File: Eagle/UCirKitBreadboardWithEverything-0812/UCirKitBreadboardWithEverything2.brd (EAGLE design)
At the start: 72.8 x 99.4 mm, 900 parts

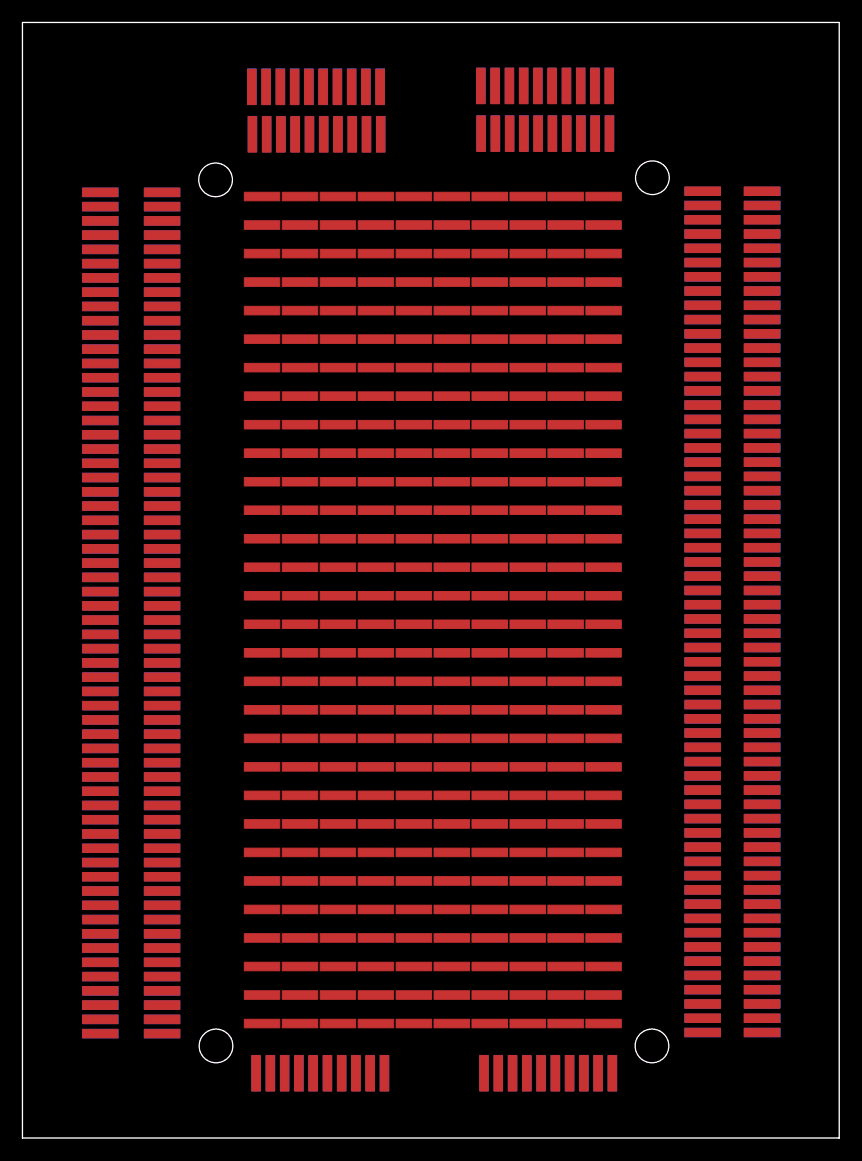
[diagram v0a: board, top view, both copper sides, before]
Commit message: UCirKitEverything2Top is OK for Routing, UCirKitEverything2 is not OK. Look for UCirKitEverything2 for Bottom part
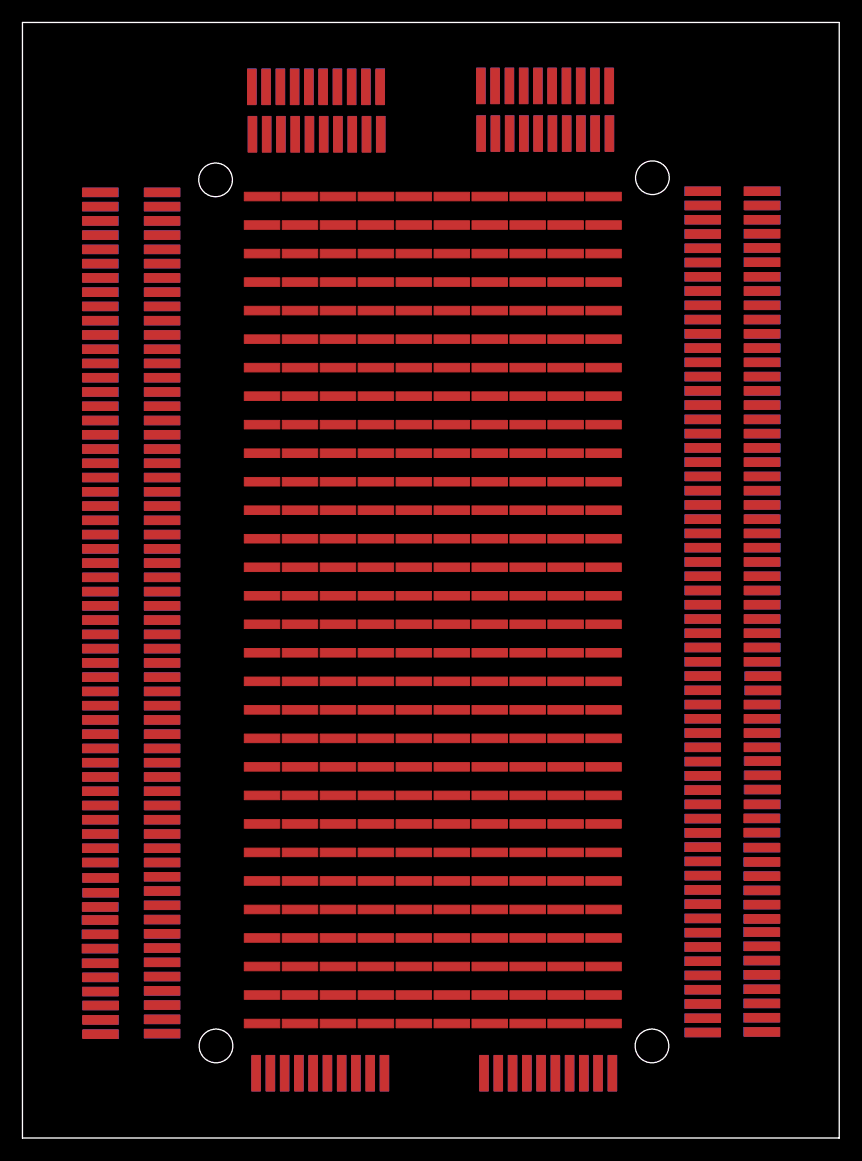
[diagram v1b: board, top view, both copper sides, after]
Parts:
- moved JP1080 16.5 mm to (65.8, 25.9), turned to 180 degrees
- moved JP780 16.5 mm to (65.9, 25.9), turned to 180 degrees
- moved JP1079 13.9 mm to (65.8, 24.6), turned to 180 degrees
- moved JP779 13.9 mm to (65.9, 24.6), turned to 180 degrees
- moved JP1069 13.9 mm to (65.8, 9.45), turned to 180 degrees
- moved JP769 13.9 mm to (65.9, 9.45), turned to 180 degrees
- moved JP1065 13.9 mm to (65.8, 14.5), turned to 180 degrees
- moved JP765 13.9 mm to (65.9, 14.5), turned to 180 degrees
- moved JP720 12.5 mm to (6.97, 21.8), turned to 180 degrees
- moved JP1140 12.5 mm to (6.94, 21.8), turned to 180 degrees
- moved JP1078 11.4 mm to (65.8, 23.3), turned to 180 degrees
- moved JP778 11.4 mm to (65.9, 23.3), turned to 180 degrees
- moved JP1070 11.4 mm to (65.8, 10.7), turned to 180 degrees
- moved JP770 11.4 mm to (65.9, 10.7), turned to 180 degrees
- moved JP1066 11.4 mm to (65.8, 15.8), turned to 180 degrees
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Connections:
- new net 0_1439897169: JP301.P$3, JP841.P$3
- new net 0_1439897178: JP311.P$3, JP843.P$3
- new net 0_1439897188: JP321.P$3, JP845.P$3
- new net 0_1439897194: JP310.P$3, JP781.P$3
- new net 0_1439897209: JP320.P$3, JP783.P$3
- new net 0_1439897217: JP330.P$3, JP785.P$3
- new net 0_1439897230: JP340.P$3, JP787.P$3
- new net 0_1439897238: JP350.P$3, JP789.P$3
- new net 0_1439897247: JP360.P$3, JP791.P$3
- new net 0_1439897254: JP370.P$3, JP793.P$3
- new net 0_1439897261: JP380.P$3, JP795.P$3
- new net 0_1439897267: JP390.P$3, JP797.P$3
- new net 0_1439897281: JP600.P$3, JP839.P$3
- new net 0_1439897288: JP590.P$3, JP837.P$3
- new net 0_1439897294: JP580.P$3, JP835.P$3
- new net 0_1439897300: JP591.P$3, JP899.P$3
- new net 0_1439897307: JP581.P$3, JP897.P$3
- new net 0_1439897312: JP571.P$3, JP895.P$3
- new net 0_1439897321: JP561.P$3, JP893.P$3
- new net 0_1439897329: JP551.P$3, JP891.P$3
- new net 0_1439897335: JP541.P$3, JP889.P$3
- new net 0_1439897341: JP531.P$3, JP887.P$3
- new net 0_1439897349: JP521.P$3, JP885.P$3
- new net 0_1439897354: JP570.P$3, JP833.P$3
- new net 0_1439897362: JP560.P$3, JP831.P$3
- new net 0_1439897369: JP550.P$3, JP829.P$3
- new net 0_1439897383: JP540.P$3, JP827.P$3
- new net 0_1439897389: JP530.P$3, JP825.P$3
- new net 0_1439897395: JP511.P$3, JP883.P$3
- new net 0_1439897401: JP501.P$3, JP881.P$3
- new net 0_1439897407: JP491.P$3, JP879.P$3
- new net 0_1439897412: JP481.P$3, JP877.P$3
- new net 0_1439897418: JP471.P$3, JP875.P$3
- new net 0_1439897423: JP461.P$3, JP873.P$3
- new net 0_1439897429: JP451.P$3, JP871.P$3
- new net 0_1439897436: JP520.P$3, JP823.P$3
- new net 0_1439897442: JP510.P$3, JP821.P$3
- new net 0_1439897448: JP500.P$3, JP819.P$3
- new net 0_1439897454: JP490.P$3, JP817.P$3
- new net 0_1439897461: JP480.P$3, JP815.P$3
- new net 0_1439897467: JP470.P$3, JP813.P$3
- new net 0_1439897473: JP460.P$3, JP811.P$3
- new net 0_1439897480: JP450.P$3, JP809.P$3
- new net 0_1439897485: JP441.P$3, JP869.P$3
- new net 0_1439897491: JP431.P$3, JP867.P$3
- new net 0_1439897496: JP421.P$3, JP865.P$3
- new net 0_1439897505: JP411.P$3, JP863.P$3
- new net 0_1439897514: JP401.P$3, JP861.P$3
- new net 0_1439897520: JP440.P$3, JP807.P$3
- new net 0_1439897527: JP430.P$3, JP805.P$3
- new net 0_1439897534: JP420.P$3, JP803.P$3
- new net 0_1439897539: JP410.P$3, JP801.P$3
- new net 0_1439897546: JP400.P$3, JP799.P$3
- new net 0_1439897614: JP391.P$3, JP859.P$3
- new net 0_1439897622: JP381.P$3, JP857.P$3
- new net 0_1439897631: JP371.P$3, JP855.P$3
- new net 0_1439897637: JP361.P$3, JP853.P$3
- new net 0_1439897643: JP351.P$3, JP851.P$3
- new net 0_1439897654: JP331.P$3, JP847.P$3
- new net 0_1439897660: JP341.P$3, JP849.P$3
- new net 0_1439897711: JP593.P$3, JP651.P$3
- new net 0_1439897726: JP597.P$3, JP641.P$3
- new net 0_1439897746: JP303.P$3, JP621.P$3
- new net 0_1439897770: JP307.P$3, JP601.P$3
- new net 0_1439897792: JP363.P$3, JP661.P$3
- new net 0_1439897815: JP378.P$3, JP721.P$3
- new net 0_1439897831: JP473.P$3, JP695.P$3
- new net 0_1439897845: JP488.P$3, JP757.P$3
- new net 0_1439897966: JP423.P$3, JP677.P$3
- new net 0_1439897993: JP428.P$3, JP737.P$3
- new net 10_1439897746: JP333.P$3, JP631.P$3
- new net 10_1439897770: JP326.P$3, JP611.P$3
- new net 10_1439897792: JP375.P$3, JP671.P$3
- new net 10_1439897815: JP376.P$3, JP731.P$3
- new net 10_1439897831: JP524.P$3, JP705.P$3
- new net 10_1439897845: JP537.P$3, JP767.P$3
- new net 10_1439897966: JP474.P$3, JP687.P$3
- new net 10_1439897993: JP467.P$3, JP747.P$3
- new net 11_1439897746: JP343.P$3, JP632.P$3
- new net 11_1439897770: JP336.P$3, JP612.P$3
- new net 11_1439897792: JP414.P$3, JP672.P$3
- new net 11_1439897815: JP417.P$3, JP732.P$3
- new net 11_1439897831: JP534.P$3, JP706.P$3
- new net 11_1439897845: JP527.P$3, JP768.P$3
- new net 11_1439897966: JP435.P$3, JP688.P$3
- new net 11_1439897993: JP477.P$3, JP748.P$3
- new net 12_1439897746: JP335.P$3, JP633.P$3
- new net 12_1439897770: JP348.P$3, JP613.P$3
- new net 12_1439897792: JP385.P$3, JP673.P$3
- new net 12_1439897815: JP386.P$3, JP733.P$3
- new net 12_1439897831: JP544.P$3, JP707.P$3
- new net 12_1439897845: JP576.P$3, JP769.P$3
- new net 12_1439897966: JP445.P$3, JP689.P$3
- new net 12_1439897993: JP446.P$3, JP749.P$3
- new net 13_1439897746: JP344.P$3, JP634.P$3
- new net 13_1439897770: JP347.P$3, JP614.P$3
- new net 13_1439897792: JP395.P$3, JP674.P$3
- new net 13_1439897815: JP396.P$3, JP734.P$3
- new net 13_1439897831: JP554.P$3, JP708.P$3
- new net 13_1439897845: JP566.P$3, JP770.P$3
- new net 13_1439897966: JP455.P$3, JP690.P$3
- new net 13_1439897993: JP456.P$3, JP750.P$3
- new net 14_1439897746: JP345.P$3, JP635.P$3
- new net 14_1439897770: JP346.P$3, JP615.P$3
- new net 14_1439897792: JP405.P$3, JP675.P$3
- new net 14_1439897815: JP406.P$3, JP735.P$3
- new net 14_1439897831: JP514.P$3, JP709.P$3
- new net 14_1439897845: JP556.P$3, JP771.P$3
- new net 14_1439897966: JP465.P$3, JP691.P$3
- new net 14_1439897993: JP466.P$3, JP751.P$3
- new net 15_1439897746: JP353.P$3, JP636.P$3
- new net 15_1439897770: JP358.P$3, JP616.P$3
- new net 15_1439897792: JP415.P$3, JP676.P$3
- new net 15_1439897815: JP416.P$3, JP736.P$3
- new net 15_1439897831: JP504.P$3, JP710.P$3
- new net 15_1439897845: JP546.P$3, JP772.P$3
- new net 15_1439897966: JP475.P$3, JP692.P$3
- new net 15_1439897993: JP476.P$3, JP752.P$3
- new net 16_1439897746: JP354.P$3, JP637.P$3
- new net 16_1439897770: JP357.P$3, JP617.P$3
- new net 16_1439897831: JP545.P$3, JP711.P$3
- new net 16_1439897845: JP517.P$3, JP773.P$3
- new net 16_1439897966: JP485.P$3, JP693.P$3
- new net 16_1439897993: JP486.P$3, JP753.P$3
- new net 17_1439897746: JP355.P$3, JP638.P$3
- new net 17_1439897770: JP356.P$3, JP618.P$3
- new net 17_1439897831: JP555.P$3, JP712.P$3
- new net 17_1439897845: JP507.P$3, JP774.P$3
- new net 17_1439897966: JP425.P$3, JP694.P$3
- new net 17_1439897993: JP496.P$3, JP754.P$3
- new net 18_1439897746: JP364.P$3, JP639.P$3
- new net 18_1439897770: JP368.P$3, JP619.P$3
- new net 18_1439897831: JP565.P$3, JP713.P$3
- new net 18_1439897845: JP536.P$3, JP775.P$3
- new net 18_1439897993: JP436.P$3, JP755.P$3
- new net 19_1439897746: JP365.P$3, JP640.P$3
- new net 19_1439897770: JP367.P$3, JP620.P$3
- new net 19_1439897831: JP535.P$3, JP714.P$3
- new net 19_1439897845: JP497.P$3, JP776.P$3
- new net 19_1439897993: JP426.P$3, JP756.P$3
- new net 1_1439897169: JP302.P$3, JP842.P$3
- new net 1_1439897178: JP312.P$3, JP844.P$3
- new net 1_1439897188: JP322.P$3, JP846.P$3
- new net 1_1439897194: JP309.P$3, JP782.P$3
- new net 1_1439897209: JP319.P$3, JP784.P$3
- new net 1_1439897217: JP329.P$3, JP786.P$3
- new net 1_1439897230: JP339.P$3, JP788.P$3
- new net 1_1439897238: JP349.P$3, JP790.P$3
- new net 1_1439897247: JP359.P$3, JP792.P$3
- new net 1_1439897254: JP369.P$3, JP794.P$3
- new net 1_1439897261: JP379.P$3, JP796.P$3
- new net 1_1439897267: JP389.P$3, JP798.P$3
- new net 1_1439897281: JP599.P$3, JP840.P$3
- new net 1_1439897288: JP589.P$3, JP838.P$3
- new net 1_1439897294: JP579.P$3, JP836.P$3
- new net 1_1439897300: JP592.P$3, JP900.P$3
- new net 1_1439897307: JP582.P$3, JP898.P$3
- new net 1_1439897312: JP572.P$3, JP896.P$3
- new net 1_1439897321: JP562.P$3, JP894.P$3
- new net 1_1439897329: JP552.P$3, JP892.P$3
- new net 1_1439897335: JP542.P$3, JP890.P$3
- new net 1_1439897341: JP532.P$3, JP888.P$3
- new net 1_1439897349: JP522.P$3, JP886.P$3
- new net 1_1439897354: JP569.P$3, JP834.P$3
- new net 1_1439897362: JP559.P$3, JP832.P$3
- new net 1_1439897369: JP549.P$3, JP830.P$3
- new net 1_1439897383: JP539.P$3, JP828.P$3
- new net 1_1439897389: JP529.P$3, JP826.P$3
- new net 1_1439897395: JP512.P$3, JP884.P$3
- new net 1_1439897401: JP502.P$3, JP882.P$3
- new net 1_1439897407: JP492.P$3, JP880.P$3
- new net 1_1439897412: JP482.P$3, JP878.P$3
- new net 1_1439897418: JP472.P$3, JP876.P$3
- new net 1_1439897423: JP462.P$3, JP874.P$3
- new net 1_1439897429: JP452.P$3, JP872.P$3
- new net 1_1439897436: JP519.P$3, JP824.P$3
- new net 1_1439897442: JP509.P$3, JP822.P$3
- new net 1_1439897448: JP499.P$3, JP820.P$3
- new net 1_1439897454: JP489.P$3, JP818.P$3
- new net 1_1439897461: JP479.P$3, JP816.P$3
- new net 1_1439897467: JP469.P$3, JP814.P$3
- new net 1_1439897473: JP459.P$3, JP812.P$3
- new net 1_1439897480: JP449.P$3, JP810.P$3
- new net 1_1439897485: JP442.P$3, JP870.P$3
- new net 1_1439897491: JP432.P$3, JP868.P$3
- new net 1_1439897496: JP422.P$3, JP866.P$3
- new net 1_1439897505: JP412.P$3, JP864.P$3
- new net 1_1439897514: JP402.P$3, JP862.P$3
- new net 1_1439897520: JP439.P$3, JP808.P$3
- new net 1_1439897527: JP429.P$3, JP806.P$3
- new net 1_1439897534: JP419.P$3, JP804.P$3
- new net 1_1439897539: JP409.P$3, JP802.P$3
- new net 1_1439897546: JP399.P$3, JP800.P$3
- new net 1_1439897614: JP392.P$3, JP860.P$3
- new net 1_1439897622: JP382.P$3, JP858.P$3
- new net 1_1439897631: JP372.P$3, JP856.P$3
- new net 1_1439897637: JP362.P$3, JP854.P$3
- new net 1_1439897643: JP352.P$3, JP852.P$3
- new net 1_1439897654: JP332.P$3, JP848.P$3
- new net 1_1439897660: JP342.P$3, JP850.P$3
- new net 1_1439897711: JP583.P$3, JP652.P$3
- new net 1_1439897726: JP598.P$3, JP642.P$3
- new net 1_1439897746: JP304.P$3, JP622.P$3
- new net 1_1439897770: JP308.P$3, JP602.P$3
- new net 1_1439897792: JP373.P$3, JP662.P$3
- new net 1_1439897815: JP388.P$3, JP722.P$3
- new net 1_1439897831: JP483.P$3, JP696.P$3
- new net 1_1439897845: JP498.P$3, JP758.P$3
- new net 1_1439897966: JP433.P$3, JP678.P$3
- new net 1_1439897993: JP438.P$3, JP738.P$3
- new net 20_1439897831: JP525.P$3, JP715.P$3
- new net 20_1439897845: JP526.P$3, JP777.P$3
- new net 21_1439897831: JP494.P$3, JP716.P$3
- new net 21_1439897845: JP487.P$3, JP778.P$3
- new net 22_1439897831: JP515.P$3, JP717.P$3
- new net 22_1439897845: JP516.P$3, JP779.P$3
- new net 23_1439897831: JP505.P$3, JP718.P$3
- new net 23_1439897845: JP506.P$3, JP780.P$3
- new net 24_1439897831: JP484.P$3, JP719.P$3
- new net 25_1439897831: JP495.P$3, JP720.P$3
- new net 2_1439897711: JP594.P$3, JP653.P$3
- new net 2_1439897726: JP596.P$3, JP643.P$3
- new net 2_1439897746: JP313.P$3, JP623.P$3
- new net 2_1439897770: JP306.P$3, JP603.P$3
- new net 2_1439897792: JP383.P$3, JP663.P$3
- new net 2_1439897815: JP377.P$3, JP723.P$3
- new net 2_1439897831: JP493.P$3, JP697.P$3
- new net 2_1439897845: JP508.P$3, JP759.P$3
- new net 2_1439897966: JP443.P$3, JP679.P$3
- new net 2_1439897993: JP448.P$3, JP739.P$3
- new net 3_1439897711: JP584.P$3, JP654.P$3
- new net 3_1439897726: JP588.P$3, JP644.P$3
- new net 3_1439897746: JP314.P$3, JP624.P$3
- new net 3_1439897770: JP318.P$3, JP604.P$3
- new net 3_1439897792: JP374.P$3, JP664.P$3
- new net 3_1439897815: JP398.P$3, JP724.P$3
- new net 3_1439897831: JP503.P$3, JP698.P$3
- new net 3_1439897845: JP518.P$3, JP760.P$3
- new net 3_1439897966: JP424.P$3, JP680.P$3
- new net 3_1439897993: JP427.P$3, JP740.P$3
- new net 4_1439897711: JP573.P$3, JP655.P$3
- new net 4_1439897726: JP587.P$3, JP645.P$3
- new net 4_1439897746: JP305.P$3, JP625.P$3
- new net 4_1439897770: JP317.P$3, JP605.P$3
- new net 4_1439897792: JP393.P$3, JP665.P$3
- new net 4_1439897815: JP387.P$3, JP725.P$3
- new net 4_1439897831: JP513.P$3, JP699.P$3
- new net 4_1439897845: JP528.P$3, JP761.P$3
- new net 4_1439897966: JP453.P$3, JP681.P$3
- new net 4_1439897993: JP458.P$3, JP741.P$3
- new net 5_1439897711: JP595.P$3, JP656.P$3
- new net 5_1439897726: JP578.P$3, JP646.P$3
- new net 5_1439897746: JP315.P$3, JP626.P$3
- new net 5_1439897770: JP328.P$3, JP606.P$3
- new net 5_1439897792: JP384.P$3, JP666.P$3
- new net 5_1439897815: JP366.P$3, JP726.P$3
- new net 5_1439897831: JP523.P$3, JP700.P$3
- new net 5_1439897845: JP538.P$3, JP762.P$3
- new net 5_1439897966: JP434.P$3, JP682.P$3
- new net 5_1439897993: JP437.P$3, JP742.P$3
- new net 6_1439897711: JP585.P$3, JP657.P$3
- new net 6_1439897726: JP577.P$3, JP647.P$3
- new net 6_1439897746: JP323.P$3, JP627.P$3
- new net 6_1439897770: JP327.P$3, JP607.P$3
- new net 6_1439897792: JP403.P$3, JP667.P$3
- new net 6_1439897815: JP408.P$3, JP727.P$3
- new net 6_1439897831: JP533.P$3, JP701.P$3
- new net 6_1439897845: JP548.P$3, JP763.P$3
- new net 6_1439897966: JP463.P$3, JP683.P$3
- new net 6_1439897993: JP468.P$3, JP743.P$3
- new net 7_1439897711: JP574.P$3, JP658.P$3
- new net 7_1439897726: JP568.P$3, JP648.P$3
- new net 7_1439897746: JP324.P$3, JP628.P$3
- new net 7_1439897770: JP338.P$3, JP608.P$3
- new net 7_1439897792: JP394.P$3, JP668.P$3
- new net 7_1439897815: JP397.P$3, JP728.P$3
- new net 7_1439897831: JP543.P$3, JP702.P$3
- new net 7_1439897845: JP558.P$3, JP764.P$3
- new net 7_1439897966: JP444.P$3, JP684.P$3
- new net 7_1439897993: JP447.P$3, JP744.P$3
- new net 8_1439897711: JP575.P$3, JP659.P$3
- new net 8_1439897726: JP586.P$3, JP649.P$3
- new net 8_1439897746: JP325.P$3, JP629.P$3
- new net 8_1439897770: JP316.P$3, JP609.P$3
- new net 8_1439897792: JP413.P$3, JP669.P$3
- new net 8_1439897815: JP418.P$3, JP729.P$3
- new net 8_1439897831: JP553.P$3, JP703.P$3
- new net 8_1439897845: JP557.P$3, JP765.P$3
- new net 8_1439897966: JP454.P$3, JP685.P$3
- new net 8_1439897993: JP478.P$3, JP745.P$3
- new net 9_1439897711: JP564.P$3, JP660.P$3
- new net 9_1439897726: JP567.P$3, JP650.P$3
- new net 9_1439897746: JP334.P$3, JP630.P$3
- new net 9_1439897770: JP337.P$3, JP610.P$3
- new net 9_1439897792: JP404.P$3, JP670.P$3
- new net 9_1439897815: JP407.P$3, JP730.P$3
- new net 9_1439897831: JP563.P$3, JP704.P$3
- new net 9_1439897845: JP547.P$3, JP766.P$3
- new net 9_1439897966: JP464.P$3, JP686.P$3
- new net 9_1439897993: JP457.P$3, JP746.P$3
- new net CLEAN600: JP901.P$3
- new net CLEAN601: JP902.P$3
- new net CLEAN602: JP903.P$3
- new net CLEAN603: JP904.P$3
- new net CLEAN604: JP905.P$3
- new net CLEAN605: JP906.P$3
- new net CLEAN606: JP907.P$3
- new net CLEAN607: JP908.P$3
- new net CLEAN608: JP909.P$3
- new net CLEAN609: JP910.P$3
- new net CLEAN610: JP911.P$3
- new net CLEAN611: JP912.P$3
- new net CLEAN612: JP913.P$3
- new net CLEAN613: JP914.P$3
- new net CLEAN614: JP915.P$3
- new net CLEAN615: JP916.P$3
- new net CLEAN616: JP917.P$3
- new net CLEAN617: JP918.P$3
- new net CLEAN618: JP919.P$3
- new net CLEAN619: JP920.P$3
- new net CLEAN620: JP921.P$3
- new net CLEAN621: JP922.P$3
- new net CLEAN622: JP923.P$3
- new net CLEAN623: JP924.P$3
- new net CLEAN624: JP925.P$3
- new net CLEAN625: JP926.P$3
- new net CLEAN626: JP927.P$3
- new net CLEAN627: JP928.P$3
- new net CLEAN628: JP929.P$3
- new net CLEAN629: JP930.P$3
- new net CLEAN630: JP931.P$3
- new net CLEAN631: JP932.P$3
- new net CLEAN632: JP933.P$3
- new net CLEAN633: JP934.P$3
- new net CLEAN634: JP935.P$3
- new net CLEAN635: JP936.P$3
- new net CLEAN636: JP937.P$3
- new net CLEAN637: JP938.P$3
- new net CLEAN638: JP939.P$3
- new net CLEAN639: JP940.P$3
- new net CLEAN640: JP941.P$3
- new net CLEAN641: JP942.P$3
- new net CLEAN642: JP943.P$3
- new net CLEAN643: JP944.P$3
- new net CLEAN644: JP945.P$3
- new net CLEAN645: JP946.P$3
- new net CLEAN646: JP947.P$3
- new net CLEAN647: JP948.P$3
- new net CLEAN648: JP949.P$3
- new net CLEAN649: JP950.P$3
- new net CLEAN650: JP951.P$3
- new net CLEAN651: JP952.P$3
- new net CLEAN652: JP953.P$3
- new net CLEAN653: JP954.P$3
- new net CLEAN654: JP955.P$3
- new net CLEAN655: JP956.P$3
- new net CLEAN656: JP957.P$3
- new net CLEAN657: JP958.P$3
- new net CLEAN658: JP959.P$3
- new net CLEAN659: JP960.P$3
- new net CLEAN660: JP961.P$3
- new net CLEAN661: JP962.P$3
- new net CLEAN662: JP963.P$3
- new net CLEAN663: JP964.P$3
- new net CLEAN664: JP965.P$3
- new net CLEAN665: JP966.P$3
- new net CLEAN666: JP967.P$3
- new net CLEAN667: JP968.P$3
- new net CLEAN668: JP969.P$3
- new net CLEAN669: JP970.P$3
- new net CLEAN670: JP971.P$3
- new net CLEAN671: JP972.P$3
- new net CLEAN672: JP973.P$3
- new net CLEAN673: JP974.P$3
- new net CLEAN674: JP975.P$3
- new net CLEAN675: JP976.P$3
- new net CLEAN676: JP977.P$3
- new net CLEAN677: JP978.P$3
- new net CLEAN678: JP979.P$3
- new net CLEAN679: JP980.P$3
- new net CLEAN680: JP981.P$3
- new net CLEAN681: JP982.P$3
- new net CLEAN682: JP983.P$3
- new net CLEAN683: JP984.P$3
- new net CLEAN684: JP985.P$3
- new net CLEAN685: JP986.P$3
- new net CLEAN686: JP987.P$3
- new net CLEAN687: JP988.P$3
- new net CLEAN688: JP989.P$3
- new net CLEAN689: JP990.P$3
- new net CLEAN690: JP991.P$3
- new net CLEAN691: JP992.P$3
- new net CLEAN692: JP993.P$3
- new net CLEAN693: JP994.P$3
- new net CLEAN694: JP995.P$3
- new net CLEAN695: JP996.P$3
- new net CLEAN696: JP997.P$3
- new net CLEAN697: JP998.P$3
- new net CLEAN698: JP999.P$3
- new net CLEAN699: JP1000.P$3
- new net CLEAN700: JP1001.P$3
- new net CLEAN701: JP1002.P$3
- new net CLEAN702: JP1003.P$3
- new net CLEAN703: JP1004.P$3
- new net CLEAN704: JP1005.P$3
- new net CLEAN705: JP1006.P$3
- new net CLEAN706: JP1007.P$3
- new net CLEAN707: JP1008.P$3
- new net CLEAN708: JP1009.P$3
- new net CLEAN709: JP1010.P$3
- new net CLEAN710: JP1011.P$3
- new net CLEAN711: JP1012.P$3
- new net CLEAN712: JP1013.P$3
- new net CLEAN713: JP1014.P$3
- new net CLEAN714: JP1015.P$3
- new net CLEAN715: JP1016.P$3
- new net CLEAN716: JP1017.P$3
- new net CLEAN717: JP1018.P$3
- new net CLEAN718: JP1019.P$3
- new net CLEAN719: JP1020.P$3
- new net CLEAN720: JP1021.P$3
- new net CLEAN721: JP1022.P$3
- new net CLEAN722: JP1023.P$3
- new net CLEAN723: JP1024.P$3
- new net CLEAN724: JP1025.P$3
- new net CLEAN725: JP1026.P$3
- new net CLEAN726: JP1027.P$3
- new net CLEAN727: JP1028.P$3
- new net CLEAN728: JP1029.P$3
- new net CLEAN729: JP1030.P$3
- new net CLEAN730: JP1031.P$3
- new net CLEAN731: JP1032.P$3
- new net CLEAN732: JP1033.P$3
- new net CLEAN733: JP1034.P$3
- new net CLEAN734: JP1035.P$3
- new net CLEAN735: JP1036.P$3
- new net CLEAN736: JP1037.P$3
- new net CLEAN737: JP1038.P$3
- new net CLEAN738: JP1039.P$3
- new net CLEAN739: JP1040.P$3
- new net CLEAN740: JP1041.P$3
- new net CLEAN741: JP1042.P$3
- new net CLEAN742: JP1043.P$3
- new net CLEAN743: JP1044.P$3
- new net CLEAN744: JP1045.P$3
- new net CLEAN745: JP1046.P$3
- new net CLEAN746: JP1047.P$3
- new net CLEAN747: JP1048.P$3
- new net CLEAN748: JP1049.P$3
- new net CLEAN749: JP1050.P$3
- new net CLEAN750: JP1051.P$3
- new net CLEAN751: JP1052.P$3
- new net CLEAN752: JP1053.P$3
- new net CLEAN753: JP1054.P$3
- new net CLEAN754: JP1055.P$3
- new net CLEAN755: JP1056.P$3
- new net CLEAN756: JP1057.P$3
- new net CLEAN757: JP1058.P$3
- new net CLEAN758: JP1059.P$3
- new net CLEAN759: JP1060.P$3
- new net CLEAN760: JP1061.P$3
- new net CLEAN761: JP1062.P$3
- new net CLEAN762: JP1063.P$3
- new net CLEAN763: JP1064.P$3
- new net CLEAN764: JP1065.P$3
- new net CLEAN765: JP1066.P$3
- new net CLEAN766: JP1067.P$3
- new net CLEAN767: JP1068.P$3
- new net CLEAN768: JP1069.P$3
- new net CLEAN769: JP1070.P$3
- new net CLEAN770: JP1071.P$3
- new net CLEAN771: JP1072.P$3
- new net CLEAN772: JP1073.P$3
- new net CLEAN773: JP1074.P$3
- new net CLEAN774: JP1075.P$3
- new net CLEAN775: JP1076.P$3
- new net CLEAN776: JP1077.P$3
- new net CLEAN777: JP1078.P$3
- new net CLEAN778: JP1079.P$3
- new net CLEAN779: JP1080.P$3
- new net CLEAN780: JP1081.P$3
- new net CLEAN781: JP1082.P$3
- new net CLEAN782: JP1083.P$3
- new net CLEAN783: JP1084.P$3
- new net CLEAN784: JP1085.P$3
- new net CLEAN785: JP1086.P$3
- new net CLEAN786: JP1087.P$3
- new net CLEAN787: JP1088.P$3
- new net CLEAN788: JP1089.P$3
- new net CLEAN789: JP1090.P$3
- new net CLEAN790: JP1091.P$3
- new net CLEAN791: JP1092.P$3
- new net CLEAN792: JP1093.P$3
- new net CLEAN793: JP1094.P$3
- new net CLEAN794: JP1095.P$3
- new net CLEAN795: JP1096.P$3
- new net CLEAN796: JP1097.P$3
- new net CLEAN797: JP1098.P$3
- new net CLEAN798: JP1099.P$3
- new net CLEAN799: JP1100.P$3
- new net CLEAN800: JP1101.P$3
- new net CLEAN801: JP1102.P$3
- new net CLEAN802: JP1103.P$3
- new net CLEAN803: JP1104.P$3
- new net CLEAN804: JP1105.P$3
- new net CLEAN805: JP1106.P$3
- new net CLEAN806: JP1107.P$3
- new net CLEAN807: JP1108.P$3
- new net CLEAN808: JP1109.P$3
- new net CLEAN809: JP1110.P$3
- new net CLEAN810: JP1111.P$3
- new net CLEAN811: JP1112.P$3
- new net CLEAN812: JP1113.P$3
- new net CLEAN813: JP1114.P$3
- new net CLEAN814: JP1115.P$3
- new net CLEAN815: JP1116.P$3
- new net CLEAN816: JP1117.P$3
- new net CLEAN817: JP1118.P$3
- new net CLEAN818: JP1119.P$3
- new net CLEAN819: JP1120.P$3
- new net CLEAN820: JP1121.P$3
- new net CLEAN821: JP1122.P$3
- new net CLEAN822: JP1123.P$3
- new net CLEAN823: JP1124.P$3
- new net CLEAN824: JP1125.P$3
- new net CLEAN825: JP1126.P$3
- new net CLEAN826: JP1127.P$3
- new net CLEAN827: JP1128.P$3
- new net CLEAN828: JP1129.P$3
- new net CLEAN829: JP1130.P$3
- new net CLEAN830: JP1131.P$3
- new net CLEAN831: JP1132.P$3
- new net CLEAN832: JP1133.P$3
- new net CLEAN833: JP1134.P$3
- new net CLEAN834: JP1135.P$3
- new net CLEAN835: JP1136.P$3
- new net CLEAN836: JP1137.P$3
- new net CLEAN837: JP1138.P$3
- new net CLEAN838: JP1139.P$3
- new net CLEAN839: JP1140.P$3
- new net CLEAN840: JP1141.P$3
- new net CLEAN841: JP1142.P$3
- new net CLEAN842: JP1143.P$3
- new net CLEAN843: JP1144.P$3
- new net CLEAN844: JP1145.P$3
- new net CLEAN845: JP1146.P$3
- new net CLEAN846: JP1147.P$3
- new net CLEAN847: JP1148.P$3
- new net CLEAN848: JP1149.P$3
- new net CLEAN849: JP1150.P$3
- new net CLEAN850: JP1151.P$3
- new net CLEAN851: JP1152.P$3
- new net CLEAN852: JP1153.P$3
- new net CLEAN853: JP1154.P$3
- new net CLEAN854: JP1155.P$3
- new net CLEAN855: JP1156.P$3
- new net CLEAN856: JP1157.P$3
- new net CLEAN857: JP1158.P$3
- new net CLEAN858: JP1159.P$3
- new net CLEAN859: JP1160.P$3
- new net CLEAN860: JP1161.P$3
- new net CLEAN861: JP1162.P$3
- new net CLEAN862: JP1163.P$3
- new net CLEAN863: JP1164.P$3
- new net CLEAN864: JP1165.P$3
- new net CLEAN865: JP1166.P$3
- new net CLEAN866: JP1167.P$3
- new net CLEAN867: JP1168.P$3
- new net CLEAN868: JP1169.P$3
- new net CLEAN869: JP1170.P$3
- new net CLEAN870: JP1171.P$3
- new net CLEAN871: JP1172.P$3
- new net CLEAN872: JP1173.P$3
- new net CLEAN873: JP1174.P$3
- new net CLEAN874: JP1175.P$3
- new net CLEAN875: JP1176.P$3
- new net CLEAN876: JP1177.P$3
- new net CLEAN877: JP1178.P$3
- new net CLEAN878: JP1179.P$3
- new net CLEAN879: JP1180.P$3
- new net CLEAN880: JP1181.P$3
- new net CLEAN881: JP1182.P$3
- new net CLEAN882: JP1183.P$3
- new net CLEAN883: JP1184.P$3
- new net CLEAN884: JP1185.P$3
- new net CLEAN885: JP1186.P$3
- new net CLEAN886: JP1187.P$3
- new net CLEAN887: JP1188.P$3
- new net CLEAN888: JP1189.P$3
- new net CLEAN889: JP1190.P$3
- new net CLEAN890: JP1191.P$3
- new net CLEAN891: JP1192.P$3
- new net CLEAN892: JP1193.P$3
- new net CLEAN893: JP1194.P$3
- new net CLEAN894: JP1195.P$3
- new net CLEAN895: JP1196.P$3
- new net CLEAN896: JP1197.P$3
- new net CLEAN897: JP1198.P$3
- new net CLEAN898: JP1199.P$3
- new net CLEAN899: JP1200.P$3
